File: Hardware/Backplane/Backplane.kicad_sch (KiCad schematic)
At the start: 3 parts, among them U101 P2X8C4M64P, U102 TCA9548APWR

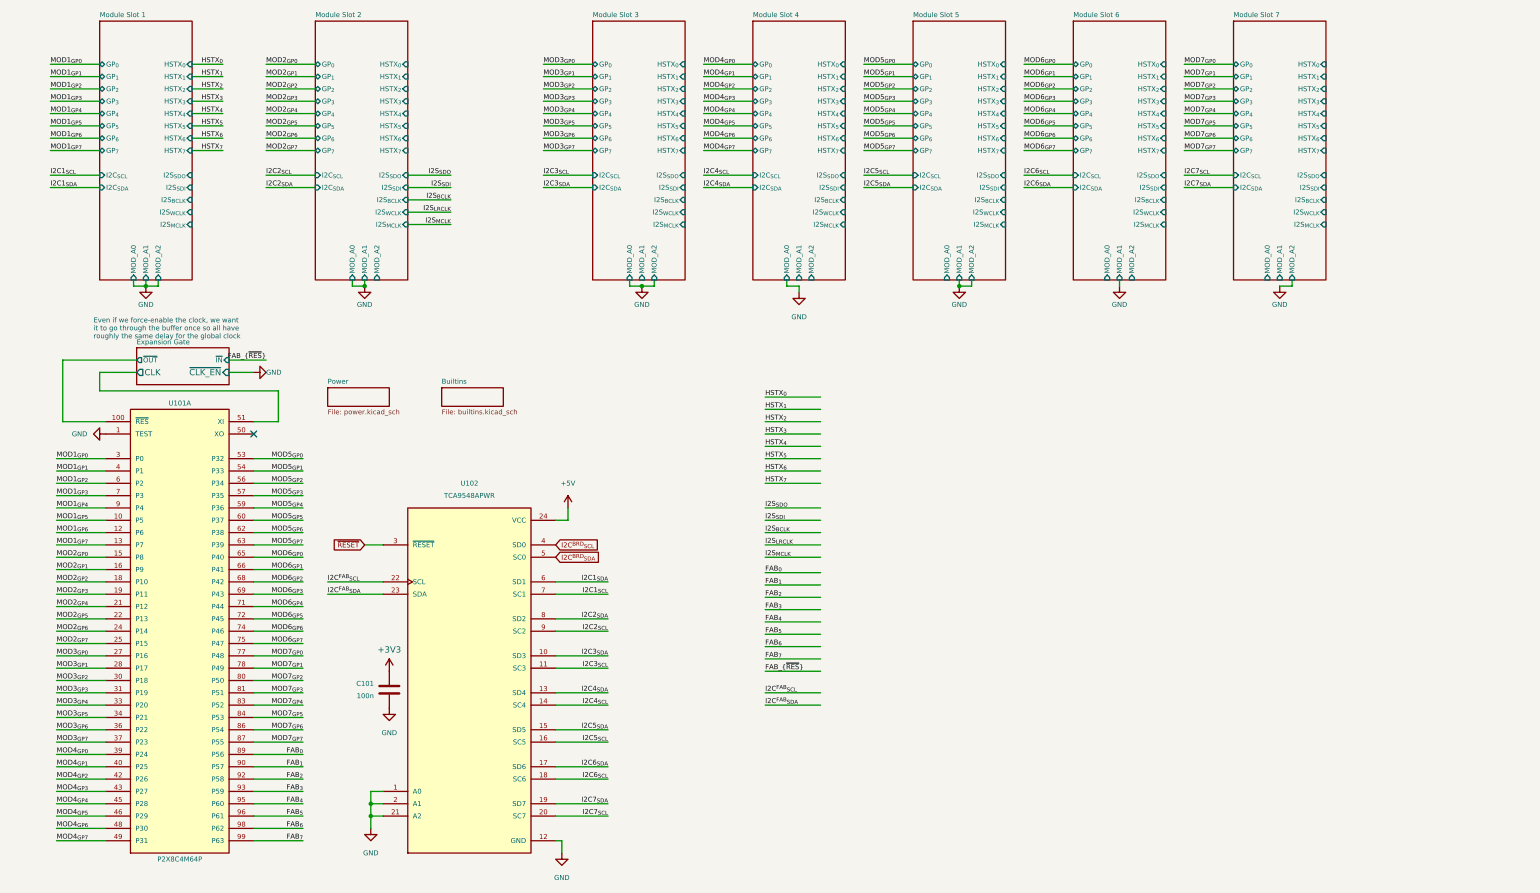
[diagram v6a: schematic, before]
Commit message: Cleans up schematic, adds clean RESET gating
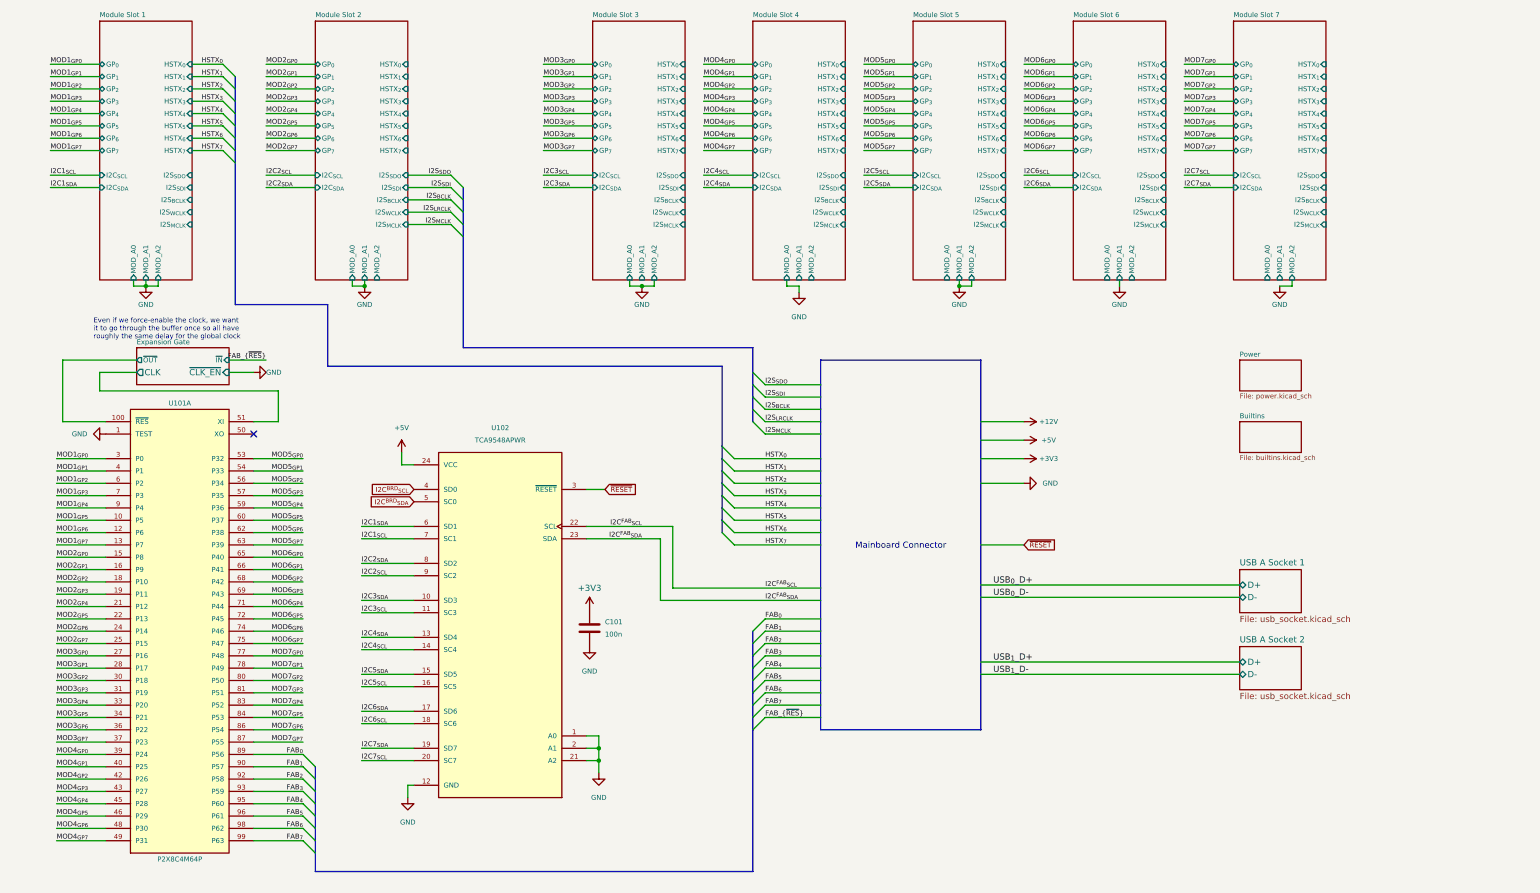
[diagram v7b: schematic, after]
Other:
- added sheet USB A Socket 1 (usb_socket.kicad_sch)
- added sheet USB A Socket 2 (usb_socket.kicad_sch)
- company: (none) -> Ashet Technologies
- title: (none) -> Ashet Home Computer Backplane
- moved on the sheet: C101, U102

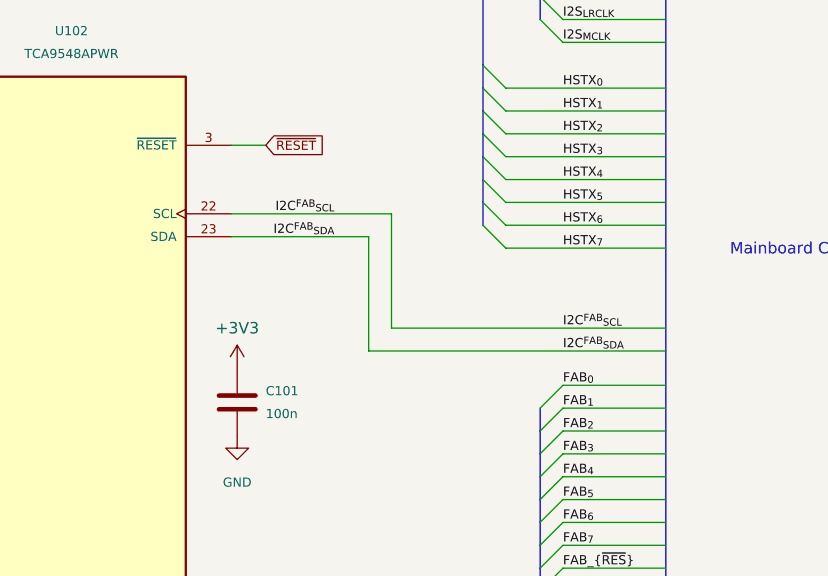
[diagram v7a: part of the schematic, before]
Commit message: Updates backplane: Improves voltage measurement dividers, replaces DS1307+ RTC with a much cheaper one, replaces 8 MHz global clock with 48 MHz global clock
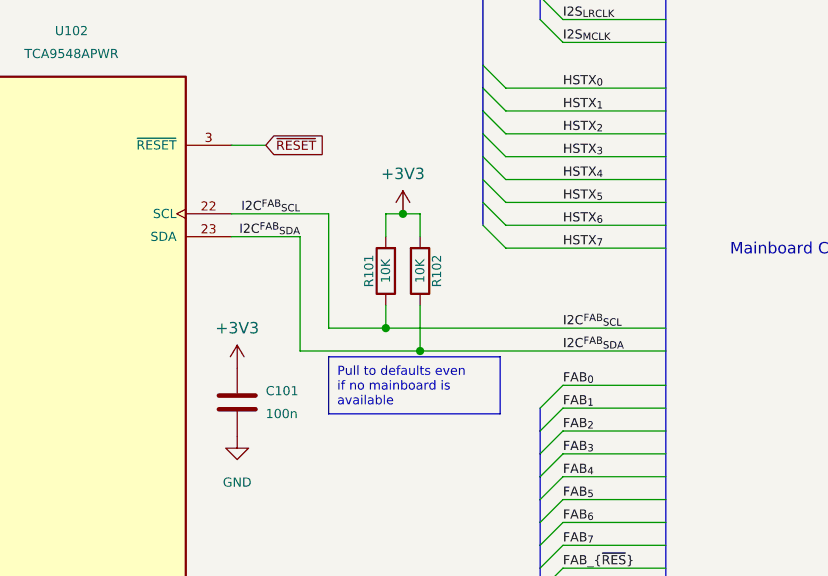
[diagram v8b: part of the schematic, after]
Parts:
- added R101, R102: 10K, Resistor_SMD:R_0603_1608Metric, symbol Device:R
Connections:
- net +3V3: now also R101.2, R102.2
- net I2C^{FAB}_{SCL}: now also R101.1
- net I2C^{FAB}_{SDA}: now also R102.1
